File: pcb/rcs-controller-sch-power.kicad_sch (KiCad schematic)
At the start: 64 parts, among them J1 00222-32051, J10 0022-232021, J2 0022-232021, J3 0022-232041, J8 00222-32051, Q1 SI7465DP-T1-E3, U2 MP26123DR-LF-Z, U3 TPS63070

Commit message: Submit for review 4.23.2025
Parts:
- removed C12, C5: 10u, Capacitor_SMD:C_0603_1608Metric, symbol Device:C_Small
- C2, C4: value 10u -> 22u

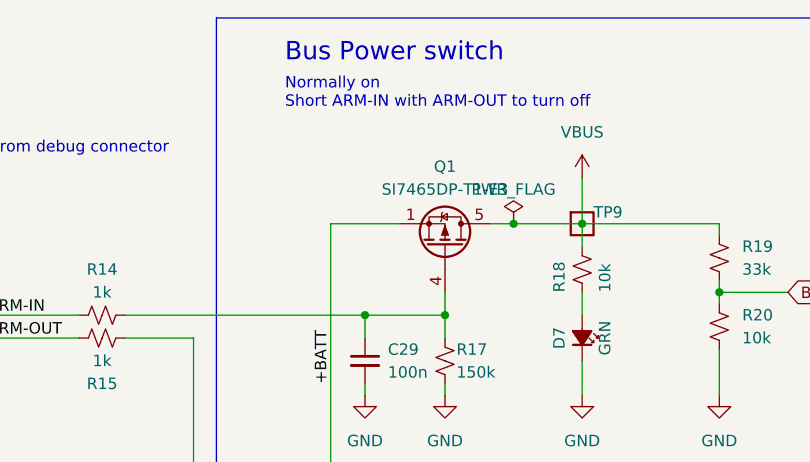
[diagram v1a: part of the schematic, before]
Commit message: Fixed BOM, fixed missing symbol and footprint libraries, stitched vias, generated Gerbers.
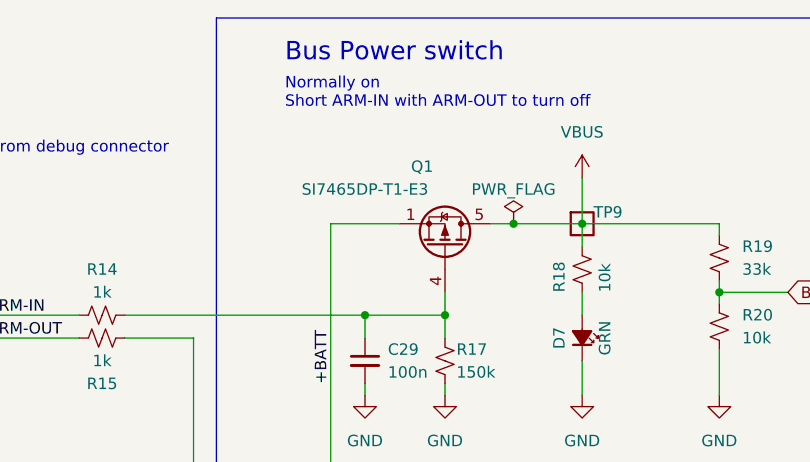
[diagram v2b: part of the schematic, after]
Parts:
- Q1: footprint PCM_Package_SON_AKL:Infineon_PG-TDSON-8 -> Package_SO:PowerPAK_SO-8_Single
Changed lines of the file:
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@@
 		(on_board yes)
 		(dnp no)
-		(fields_autoplaced yes)
 		(property "Reference" "Q1"
-			(at 321.31 63.5 90)
+			(at 318.77 63.5 90)
 			(effects
 				(font
@@
 		)
 		(property "Value" "SI7465DP-T1-E3"
-			(at 321.31 66.04 90)
+			(at 312.42 66.04 90)
 			(effects
 				(font
@@
 			)
 		)
-		(property "Footprint" "PCM_Package_SON_AKL:Infineon_PG-TDSON-8"
+		(property "Footprint" "Package_SO:PowerPAK_SO-8_Single"
 			(at 319.405 67.31 0)
 			(effects

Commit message: Push for design review 6.24
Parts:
- C14, C15, C16: DPN 490-12389-1-ND -> 445-14428-1-ND; MPN GRT21BR61E226ME13L -> C2012X5R1V226M125AC
- C2, C4: DPN 490-18663-1-ND -> 445-14428-1-ND; MPN GRM21BR61H106KE43L -> C2012X5R1V226M125AC
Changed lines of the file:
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@@
 			)
 		)
-		(property "Description" "CAP CER 22UF 25V X5R 0805"
+		(property "Description" "CAP CER 22UF 35V X5R 0805"
 			(at 293.37 133.35 0)
 			(effects
@@
 			)
 		)
-		(property "MPN" "GRT21BR61E226ME13L"
+		(property "MPN" "C2012X5R1V226M125AC"
 			(at 293.37 133.35 0)
 			(effects
@@
 			)
 		)
-		(property "DPN" "490-12389-1-ND"
+		(property "DPN" "445-14428-1-ND"
 			(at 293.37 133.35 0)
 			(effects
@@
 			)
 		)
-		(property "Description" "CAP CER 22UF 25V X5R 0805"
+		(property "Description" "CAP CER 22UF 35V X5R 0805"
 			(at 283.21 213.36 0)
 			(effects
@@
 			)
 		)
-		(property "MPN" "GRT21BR61E226ME13L"
+		(property "MPN" "C2012X5R1V226M125AC"
 			(at 283.21 213.36 0)
 			(effects
@@
 			)
 		)
-		(property "DPN" "490-12389-1-ND"
+		(property "DPN" "445-14428-1-ND"
 			(at 283.21 213.36 0)
 			(effects
@@
 			)
 		)
-		(property "Description" "CAP CER 22UF 25V X5R 0805"
+		(property "Description" "CAP CER 22UF 35V X5R 0805"
 			(at 273.05 213.36 0)
 			(effects
@@
 			)
 		)
-		(property "MPN" "GRT21BR61E226ME13L"
+		(property "MPN" "C2012X5R1V226M125AC"
 			(at 273.05 213.36 0)
 			(effects
@@
 			)
 		)
-		(property "DPN" "490-12389-1-ND"
+		(property "DPN" "445-14428-1-ND"
 			(at 273.05 213.36 0)
 			(effects
@@
 			)
 		)
-		(property "Description" "CAP CER 10UF 50V X5R 0805"
+		(property "Description" "CAP CER 22UF 35V X5R 0805"
 			(at 191.77 213.36 0)
 			(effects
@@
 			)
 		)
-		(property "DPN" "490-18663-1-ND"
+		(property "DPN" "445-14428-1-ND"
 			(at 191.77 213.36 0)
 			(effects
@@
 			)
 		)
-		(property "MPN" "GRM21BR61H106KE43L"
+		(property "MPN" "C2012X5R1V226M125AC"
 			(at 191.77 213.36 0)
 			(effects
@@
 			)
 		)
-		(property "Description" "CAP CER 10UF 50V X5R 0805"
+		(property "Description" "CAP CER 22UF 35V X5R 0805"
 			(at 181.61 213.36 0)
 			(effects
@@
 			)
 		)
-		(property "DPN" "490-18663-1-ND"
+		(property "DPN" "445-14428-1-ND"
 			(at 181.61 213.36 0)
 			(effects
@@
 			)
 		)
-		(property "MPN" "GRM21BR61H106KE43L"
+		(property "MPN" "C2012X5R1V226M125AC"
 			(at 181.61 213.36 0)
 			(effects
